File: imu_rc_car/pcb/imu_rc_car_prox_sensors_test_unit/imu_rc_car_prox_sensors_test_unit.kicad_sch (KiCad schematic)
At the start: 12 parts, among them J1 Conn_01x05_Socket

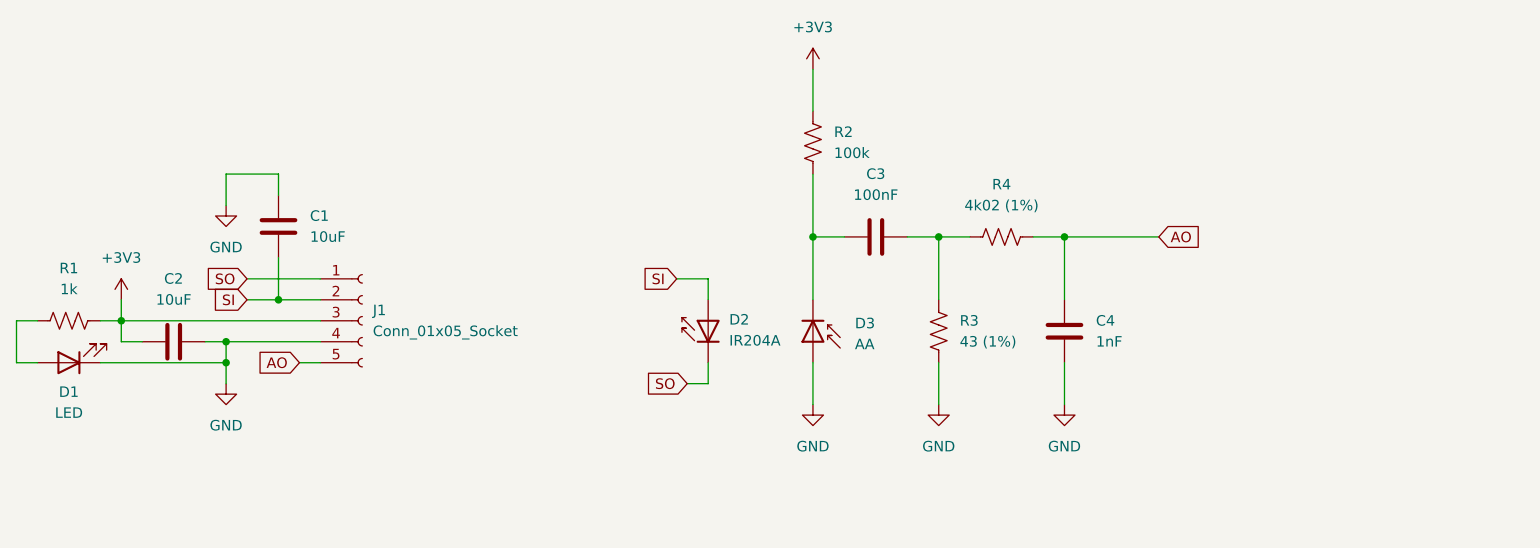
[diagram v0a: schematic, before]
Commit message: commit #24
version 2 of proximity sensor case (better results)
updated all M2 holes in pcbs to 2.4mm diameter instead of 2.2mm
updated all M3 holes in pcbs to 3.4mm diameter instead of 3.2mm
minor changes to encoder board
gerber files encoder board
first revision in hand unit
added prox sensor test unit (for test purposes)
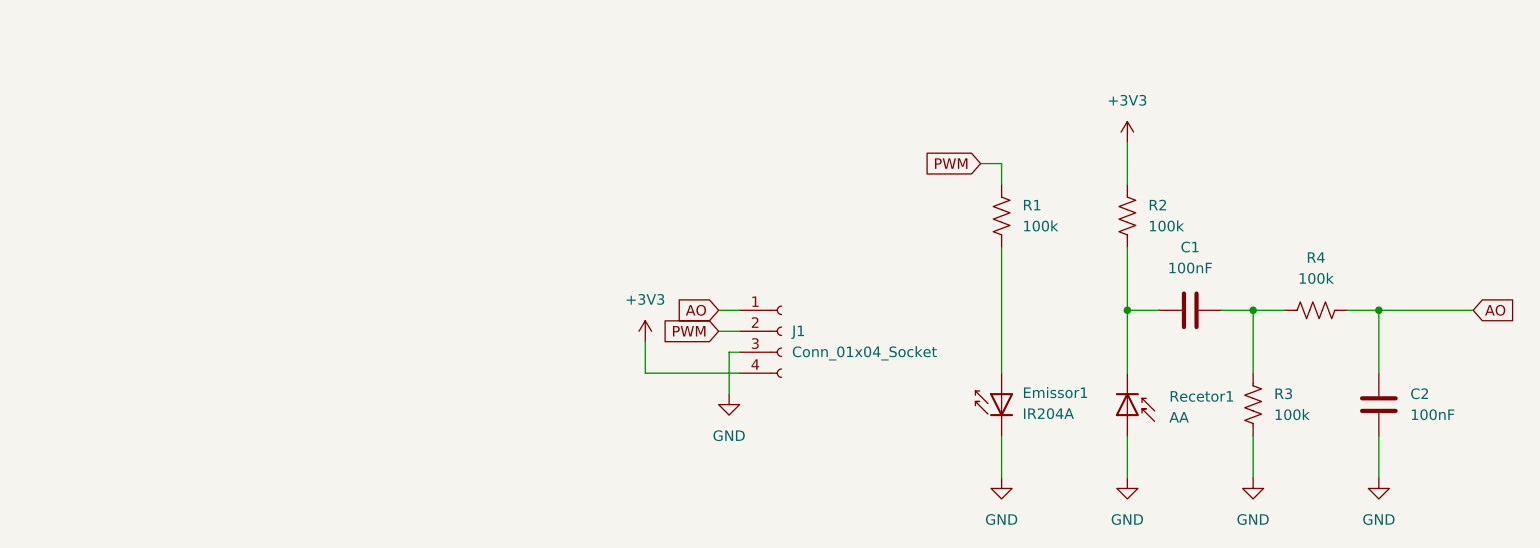
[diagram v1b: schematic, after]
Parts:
- removed C3: 100nF, Capacitor_SMD:C_0805_2012Metric, symbol Device:C
- removed C4: 1nF, Capacitor_SMD:C_0805_2012Metric, symbol Device:C
- removed D1: LED, LED_SMD:LED_0805_2012Metric, symbol Device:LED
- removed D2: IR204A, LED_THT:LED_D5.0mm_Horizontal_O1.27mm_Z3.0mm_Clear, symbol LED:IR204A
- removed D3: AA, LED_THT:LED_D5.0mm_Horizontal_O1.27mm_Z3.0mm_IRBlack, symbol Device:D_Photo
- removed J1: Conn_01x05_Socket, IMURCLibrary:JST_PH_S5B-PH-SM4-TB_1x05-1MP_P2.00mm_Horizontal, symbol Connector:Conn_01x05_Socket
- added Emissor1: IR204A, LED_THT:LED_D5.0mm_Horizontal_O1.27mm_Z3.0mm_Clear, symbol LED:IR204A
- added J1: Conn_01x04_Socket, Connector_PinHeader_2.54mm:PinHeader_1x04_P2.54mm_Horizontal, symbol Connector:Conn_01x04_Socket
- added Recetor1: AA, LED_THT:LED_D5.0mm_Horizontal_O1.27mm_Z3.0mm_IRBlack, symbol Device:D_Photo
- C1, C2: value 10uF -> 100nF; footprint Capacitor_SMD:C_0805_2012Metric -> Capacitor_THT:C_Disc_D5.0mm_W2.5mm_P5.00mm
- R1: value 1k -> 100k; footprint Resistor_SMD:R_0805_2012Metric -> Resistor_THT:R_Axial_DIN0204_L3.6mm_D1.6mm_P5.08mm_Horizontal
- R2: footprint Resistor_SMD:R_0805_2012Metric -> Resistor_THT:R_Axial_DIN0204_L3.6mm_D1.6mm_P5.08mm_Horizontal
- R3: value 43 (1%) -> 100k; footprint Resistor_SMD:R_0805_2012Metric -> Resistor_THT:R_Axial_DIN0204_L3.6mm_D1.6mm_P5.08mm_Horizontal
- R4: value 4k02 (1%) -> 100k; footprint Resistor_SMD:R_0805_2012Metric -> Resistor_THT:R_Axial_DIN0204_L3.6mm_D1.6mm_P5.08mm_Horizontal
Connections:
- net SI is gone; now on an unnamed net: C1.2
- net +3V3: now also J1.4 (Pin_4); no longer C2.2, R1.2
- net AO: now also C2.2, J1.1 (Pin_1)
- net GND: now also Emissor1.1 (K), J1.3 (Pin_3), Recetor1.2 (A); no longer C1.1
- net at R2.1: now also C1.1, Recetor1.1 (K)
- net at R1.1: now also Emissor1.2 (A)
- new net PWM: J1.2 (Pin_2), R1.2

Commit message: commit #28
added 3d file for esp32s3
progression with car pcb
minor changes prox sensors test board
final revision hand unit
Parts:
- C2: value 100nF -> 1nF
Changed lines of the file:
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@@
 (kicad_sch
-	(version 20231120)
+	(version 20250114)
 	(generator "eeschema")
-	(generator_version "8.0")
+	(generator_version "9.0")
 	(paper "A4")
 	(junction
@@
 			)
 		)
-		(property "Value" "100nF"
+		(property "Value" "1nF"
 			(at 209.55 102.8699 0)
 			(effects
@@
 		)
 	)
+	(embedded_fonts no)
 )
